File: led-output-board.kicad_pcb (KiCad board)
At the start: 2 copper layers, 29 parts, among them J1 DBT50G-9.5-2P, J10 DB301V-3.5-3P-GN, J2 Conn_02x08_Odd_Even, J3 DB301V-3.5-3P-GN, J4 DB301V-3.5-3P-GN, J5 DB301V-3.5-3P-GN, J6 DB301V-3.5-3P-GN, J7 DB301V-3.5-3P-GN, J8 DB301V-3.5-3P-GN, J9 DB301V-3.5-3P-GN, U1 SN74LVC8T245PWR

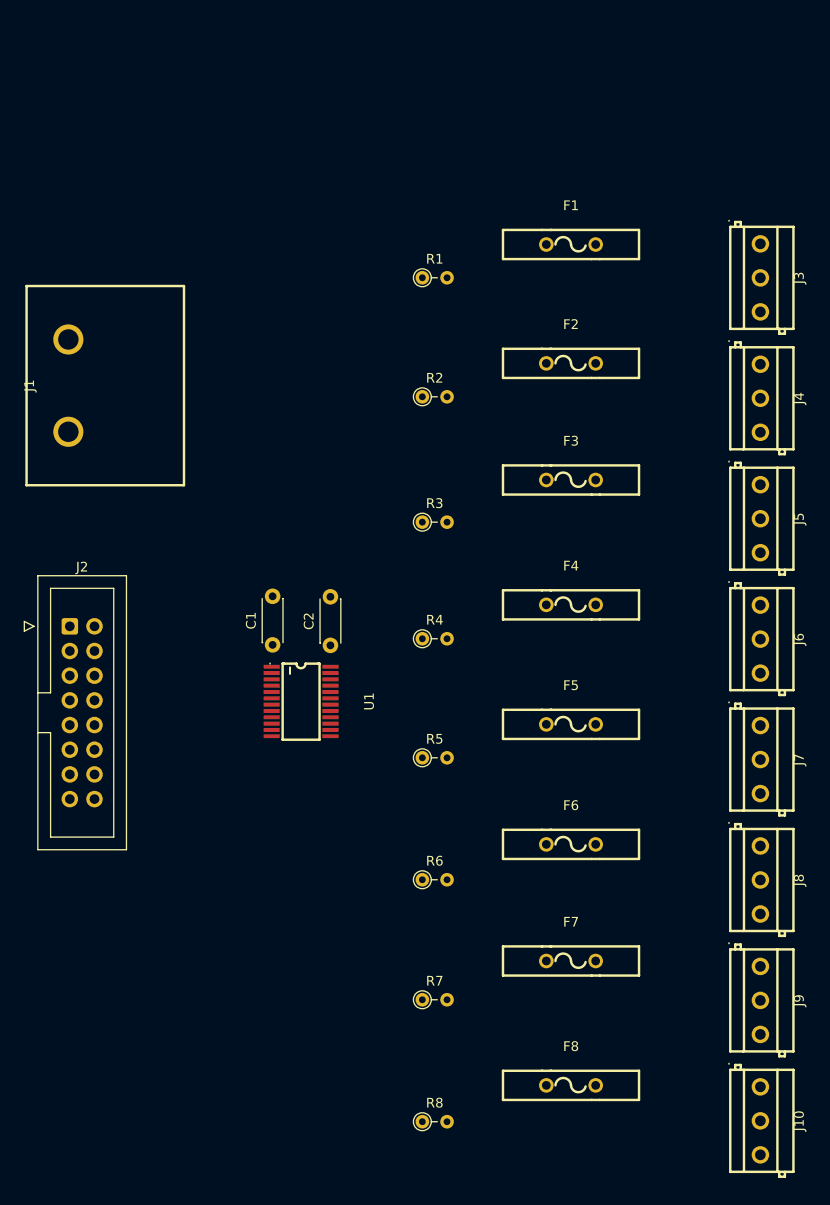
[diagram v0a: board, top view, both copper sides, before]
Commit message: Moving fuses closer
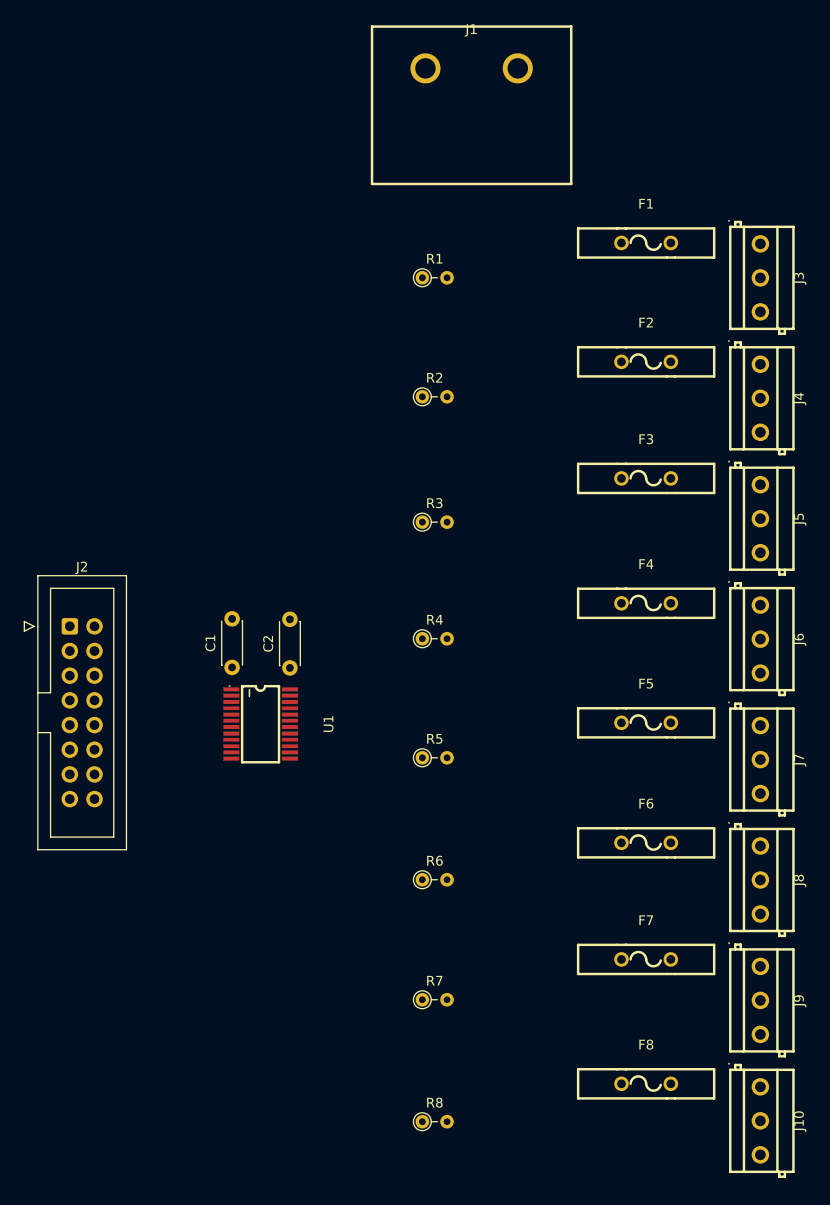
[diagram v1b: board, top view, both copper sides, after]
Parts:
- moved J1 52.8 mm to (107.9, 46.6), turned to 0 degrees
- moved F1 7.73 mm to (125.9, 64.6)
- moved F2 7.73 mm to (125.9, 76.8)
- moved F3 7.73 mm to (125.9, 88.8)
- moved F4 7.73 mm to (125.9, 101.7)
- moved F5 7.73 mm to (125.9, 114.0)
- moved F6 7.73 mm to (125.9, 126.3)
- moved F7 7.73 mm to (125.9, 138.3)
- moved F8 7.73 mm to (125.9, 151.2)
- moved C1 4.77 mm to (83.2, 108.3)
- moved C2 4.77 mm to (89.2, 108.3)
- moved U1 4.77 mm to (86.2, 114.1)
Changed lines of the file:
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@@
 	(footprint "easyeda2kicad:FUSE-TH_L14.0-W3.0-P5.08-D0.6"
 		(layer "F.Cu")
-		(at 118.1275 77.010357)
+		(at 125.86 76.85)
 		(property "Reference" "F2"
 			(at 0 -4 0)
@@
 	(footprint "easyeda2kicad:FUSE-TH_L14.0-W3.0-P5.08-D0.6"
 		(layer "F.Cu")
-		(at 118.1275 151.310357)
+		(at 125.86 151.15)
 		(property "Reference" "F8"
 			(at 0 -4 0)
@@
 	(footprint "easyeda2kicad:FUSE-TH_L14.0-W3.0-P5.08-D0.6"
 		(layer "F.Cu")
-		(at 118.1275 64.777857)
+		(at 125.86 64.6175)
 		(property "Reference" "F1"
 			(at 0 -4 0)
@@
 	(footprint "easyeda2kicad:CONN-TH_2P-P9.50_DBT50G-9.5-2P"
 		(layer "F.Cu")
-		(at 66.4 79.3 90)
+		(at 107.9 46.65)
 		(property "Reference" "J1"
-			(at 0 -4 90)
+			(at 0 -4 0)
 			(layer "F.SilkS")
 			(effects
@@
 		)
 		(property "Value" "DBT50G-9.5-2P"
-			(at 0 4 90)
+			(at 0 4 0)
 			(layer "F.Fab")
 			(effects
@@
 		)
 		(property "Datasheet" ""
-			(at 0 0 90)
+			(at 0 0 0)
 			(layer "F.Fab")
 			(hide yes)
@@
 		)
 		(property "Description" ""
-			(at 0 0 90)
+			(at 0 0 0)
 			(layer "F.Fab")
 			(hide yes)
@@
 		)
 		(property "LCSC Part" ""
-			(at 0 0 90)
+			(at 0 0 0)
 			(layer "F.Fab")
 			(hide yes)
@@
 		(duplicate_pad_numbers_are_jumpers no)
 		(fp_line
-			(start 10.25 -4.3)
-			(end -10.25 -4.3)
+			(start -10.25 -4.3)
+			(end -10.25 11.9)
 			(stroke
 				(width 0.25)
@@
 		)
 		(fp_line
-			(start -10.25 -4.3)
-			(end -10.25 11.9)
+			(start -10.25 11.9)
+			(end 10.25 11.9)
 			(stroke
 				(width 0.25)
@@
 		)
 		(fp_line
-			(start 10.25 11.9)
-			(end 10.25 -4.3)
+			(start 10.25 -4.3)
+			(end -10.25 -4.3)
 			(stroke
 				(width 0.25)
@@
 		)
 		(fp_line
-			(start -10.25 11.9)
-			(end 10.25 11.9)
+			(start 10.25 11.9)
+			(end 10.25 -4.3)
 			(stroke
 				(width 0.25)
@@
 		)
 		(fp_line
-			(start 10.25 -4.3)
-			(end 10.25 11.9)
+			(start -10.25 -4.3)
+			(end 10.25 -4.3)
 			(stroke
 				(width 0.05)
@@
 		)
 		(fp_line
-			(start -10.25 -4.3)
-			(end 10.25 -4.3)
+			(start -10.25 11.9)
+			(end -10.25 -4.3)
 			(stroke
 				(width 0.05)
@@
 		)
 		(fp_line
-			(start 10.25 11.9)
-			(end -10.25 11.9)
+			(start 10.25 -4.3)
+			(end 10.25 11.9)
 			(stroke
 				(width 0.05)
@@
 		)
 		(fp_line
-			(start -10.25 11.9)
-			(end -10.25 -4.3)
+			(start 10.25 11.9)
+			(end -10.25 11.9)
 			(stroke
 				(width 0.05)
@@
 		)
 		(fp_text user "${REFERENCE}"
-			(at 0 0 90)
+			(at 0 0 0)
 			(layer "F.Fab")
 			(effects
@@
 		)
 		(pad "1" thru_hole circle
-			(at -4.75 0 90)
+			(at -4.75 0)
 			(size 3.1 3.1)
 			(drill 2.100022)
@@
 		)
 		(pad "2" thru_hole circle
-			(at 4.75 0 90)
+			(at 4.75 0)
 			(size 3.1 3.1)
 			(drill 2.100022)
@@
 	(footprint "easyeda2kicad:FUSE-TH_L14.0-W3.0-P5.08-D0.6"
 		(layer "F.Cu")
-		(at 118.1275 89.010357)
+		(at 125.86 88.85)
 		(property "Reference" "F3"
 			(at 0 -4 0)
@@
 	(footprint "Capacitor_THT:C_Disc_D4.3mm_W1.9mm_P5.00mm"
 		(layer "F.Cu")
-		(at 87.42 105.98 90)
+		(at 83.25 108.3 90)
 		(descr "C, Disc series, Radial, pin pitch=5.00mm, diameter*width=4.3*1.9mm^2, Capacitor, http://www.vishay.com/docs/45233/krseries.pdf")
 		(tags "C Disc series Radial pin pitch 5.00mm diameter 4.3mm width 1.9mm Capacitor")
@@
 	(footprint "easyeda2kicad:FUSE-TH_L14.0-W3.0-P5.08-D0.6"
 		(layer "F.Cu")
-		(at 118.1275 101.860357)
+		(at 125.86 101.7)
 		(property "Reference" "F4"
 			(at 0 -4 0)
@@
 	(footprint "easyeda2kicad:FUSE-TH_L14.0-W3.0-P5.08-D0.6"
 		(layer "F.Cu")
-		(at 118.1275 126.510357)
+		(at 125.86 126.35)
 		(property "Reference" "F6"
 			(at 0 -4 0)
@@
 	(footprint "easyeda2kicad:TSSOP-24_L7.8-W4.4-P0.65-LS6.4-BL"
 		(layer "F.Cu")
-		(at 90.35 111.8 -90)
+		(at 86.18 114.12 -90)
 		(property "Reference" "U1"
 			(at 0 -7.023 90)
@@
 	(footprint "Capacitor_THT:C_Disc_D4.3mm_W1.9mm_P5.00mm"
 		(layer "F.Cu")
-		(at 93.37 106.03 90)
+		(at 89.2 108.35 90)
 		(descr "C, Disc series, Radial, pin pitch=5.00mm, diameter*width=4.3*1.9mm^2, Capacitor, http://www.vishay.com/docs/45233/krseries.pdf")
 		(tags "C Disc series Radial pin pitch 5.00mm diameter 4.3mm width 1.9mm Capacitor")
@@
 	(footprint "easyeda2kicad:FUSE-TH_L14.0-W3.0-P5.08-D0.6"
 		(layer "F.Cu")
-		(at 118.1275 114.160357)
+		(at 125.86 114)
 		(property "Reference" "F5"
 			(at 0 -4 0)
@@
 	(footprint "easyeda2kicad:FUSE-TH_L14.0-W3.0-P5.08-D0.6"
 		(layer "F.Cu")
-		(at 118.1275 138.510357)
+		(at 125.86 138.35)
 		(property "Reference" "F7"
 			(at 0 -4 0)

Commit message: Compacting output terminals
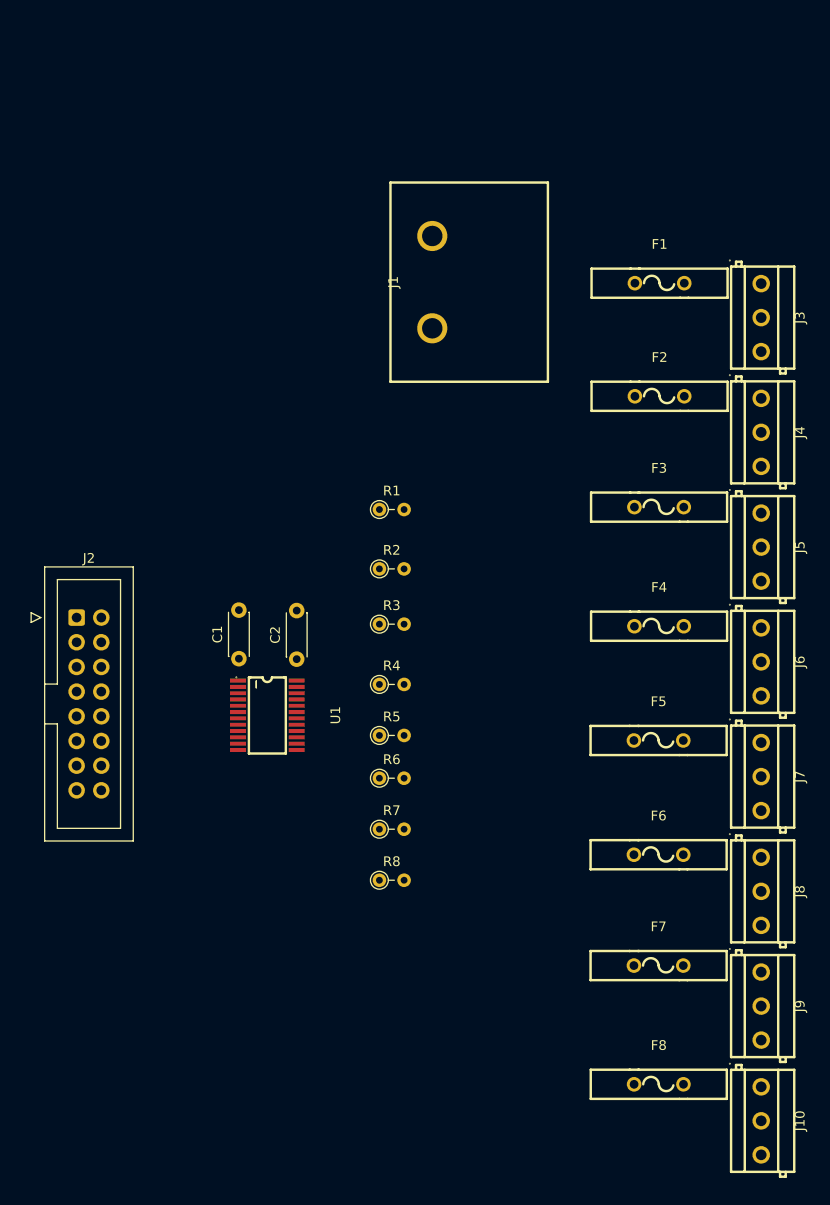
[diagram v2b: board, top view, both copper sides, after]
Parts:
- moved R8 25.2 mm to (98.4, 130.2)
- moved R1 24.3 mm to (98.4, 92.0)
- moved J1 22.4 mm to (103.8, 68.7), turned to 90 degrees
- moved R2 18.3 mm to (98.4, 98.2)
- moved R7 18.1 mm to (98.4, 125.0)
- moved R3 11.4 mm to (98.4, 103.8)
- moved R6 11.3 mm to (98.4, 119.7)
- moved R4 6.45 mm to (98.4, 110.0)
- moved R5 4.98 mm to (98.4, 115.3)
- moved F1 4.36 mm to (127.2, 68.8)
- moved J3 4.09 mm to (137.7, 72.3)
- moved F2 3.81 mm to (127.2, 80.4)
- moved J4 3.51 mm to (137.7, 84.1)
- moved F3 3.24 mm to (127.2, 91.8)
- moved J5 2.92 mm to (137.7, 95.9)
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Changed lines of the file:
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@@
 	(footprint "easyeda2kicad:FUSE-TH_L14.0-W3.0-P5.08-D0.6"
 		(layer "F.Cu")
-		(at 125.86 76.85)
+		(at 127.2425 80.396786)
 		(property "Reference" "F2"
 			(at 0 -4 0)
@@
 	(footprint "easyeda2kicad:FUSE-TH_L14.0-W3.0-P5.08-D0.6"
 		(layer "F.Cu")
-		(at 125.86 151.15)
+		(at 127.16 151.2)
 		(property "Reference" "F8"
 			(at 0 -4 0)
@@
 	(footprint "easyeda2kicad:FUSE-TH_L14.0-W3.0-P5.08-D0.6"
 		(layer "F.Cu")
-		(at 125.86 64.6175)
+		(at 127.2425 68.757143)
 		(property "Reference" "F1"
 			(at 0 -4 0)
@@
 	(footprint "Resistor_THT:R_Axial_DIN0204_L3.6mm_D1.6mm_P2.54mm_Vertical"
 		(layer "F.Cu")
-		(at 102.83 130.15)
+		(at 98.41 119.7)
 		(descr "Resistor, Axial_DIN0204 series, Axial, Vertical, pin pitch=2.54mm, 0.167W, length*diameter=3.6*1.6mm^2, http://cdn-reichelt.de/documents/datenblatt/B400/1_4W%23YAG.pdf")
 		(tags "Resistor Axial_DIN0204 series Axial Vertical pin pitch 2.54mm 0.167W length 3.6mm diameter 1.6mm")
@@
 	(footprint "Resistor_THT:R_Axial_DIN0204_L3.6mm_D1.6mm_P2.54mm_Vertical"
 		(layer "F.Cu")
-		(at 102.83 142.5)
+		(at 98.41 124.95)
 		(descr "Resistor, Axial_DIN0204 series, Axial, Vertical, pin pitch=2.54mm, 0.167W, length*diameter=3.6*1.6mm^2, http://cdn-reichelt.de/documents/datenblatt/B400/1_4W%23YAG.pdf")
 		(tags "Resistor Axial_DIN0204 series Axial Vertical pin pitch 2.54mm 0.167W length 3.6mm diameter 1.6mm")
@@
 	(footprint "Resistor_THT:R_Axial_DIN0204_L3.6mm_D1.6mm_P2.54mm_Vertical"
 		(layer "F.Cu")
-		(at 102.83 68.2)
+		(at 98.41 92.05)
 		(descr "Resistor, Axial_DIN0204 series, Axial, Vertical, pin pitch=2.54mm, 0.167W, length*diameter=3.6*1.6mm^2, http://cdn-reichelt.de/documents/datenblatt/B400/1_4W%23YAG.pdf")
 		(tags "Resistor Axial_DIN0204 series Axial Vertical pin pitch 2.54mm 0.167W length 3.6mm diameter 1.6mm")
@@
 	(footprint "Resistor_THT:R_Axial_DIN0204_L3.6mm_D1.6mm_P2.54mm_Vertical"
 		(layer "F.Cu")
-		(at 102.83 93.35)
+		(at 98.41 103.85)
 		(descr "Resistor, Axial_DIN0204 series, Axial, Vertical, pin pitch=2.54mm, 0.167W, length*diameter=3.6*1.6mm^2, http://cdn-reichelt.de/documents/datenblatt/B400/1_4W%23YAG.pdf")
 		(tags "Resistor Axial_DIN0204 series Axial Vertical pin pitch 2.54mm 0.167W length 3.6mm diameter 1.6mm")
@@
 	(footprint "Resistor_THT:R_Axial_DIN0204_L3.6mm_D1.6mm_P2.54mm_Vertical"
 		(layer "F.Cu")
-		(at 102.83 105.35)
+		(at 98.41 110.05)
 		(descr "Resistor, Axial_DIN0204 series, Axial, Vertical, pin pitch=2.54mm, 0.167W, length*diameter=3.6*1.6mm^2, http://cdn-reichelt.de/documents/datenblatt/B400/1_4W%23YAG.pdf")
 		(tags "Resistor Axial_DIN0204 series Axial Vertical pin pitch 2.54mm 0.167W length 3.6mm diameter 1.6mm")
@@
 	(footprint "easyeda2kicad:CONN-TH_DB301V-3.5-3P-GN"
 		(layer "F.Cu")
-		(at 137.6175 117.781786 -90)
+		(at 137.7 119.53449 -90)
 		(property "Reference" "J7"
 			(at 0 -4 90)
@@
 	(footprint "easyeda2kicad:CONN-TH_DB301V-3.5-3P-GN"
 		(layer "F.Cu")
-		(at 137.6175 92.996071 -90)
+		(at 137.7 95.917245 -90)
 		(property "Reference" "J5"
 			(at 0 -4 90)
@@
 	(footprint "Connector_IDC:IDC-Header_2x08_P2.54mm_Vertical"
 		(layer "F.Cu")
-		(at 66.55 104.07)
+		(at 67.25 103.17)
 		(descr "Through hole IDC box header, 2x08, 2.54mm pitch, DIN 41651 / IEC 60603-13, double rows, https://docs.google.com/spreadsheets/d/16SsEcesNF15N3Lb4niX7dcUr-NY5_MFPQhobNuNppn4/edit#gid=0")
 		(tags "Through hole vertical IDC box header THT 2x08 2.54mm double row")
@@
 	(footprint "easyeda2kicad:CONN-TH_2P-P9.50_DBT50G-9.5-2P"
 		(layer "F.Cu")
-		(at 107.9 46.65)
+		(at 103.85 68.65 90)
 		(property "Reference" "J1"
-			(at 0 -4 0)
+			(at 0 -4 90)
 			(layer "F.SilkS")
 			(effects
@@
 		)
 		(property "Value" "DBT50G-9.5-2P"
-			(at 0 4 0)
+			(at 0 4 90)
 			(layer "F.Fab")
 			(effects
@@
 		)
 		(property "Datasheet" ""
-			(at 0 0 0)
+			(at 0 0 90)
 			(layer "F.Fab")
 			(hide yes)
@@
 		)
 		(property "Description" ""
-			(at 0 0 0)
+			(at 0 0 90)
 			(layer "F.Fab")
 			(hide yes)
@@
 		)
 		(property "LCSC Part" ""
-			(at 0 0 0)
+			(at 0 0 90)
 			(layer "F.Fab")
 			(hide yes)
@@
 		(duplicate_pad_numbers_are_jumpers no)
 		(fp_line
-			(start -10.25 -4.3)
-			(end -10.25 11.9)
+			(start 10.25 -4.3)
+			(end -10.25 -4.3)
 			(stroke
 				(width 0.25)
@@
 		)
 		(fp_line
-			(start -10.25 11.9)
-			(end 10.25 11.9)
+			(start -10.25 -4.3)
+			(end -10.25 11.9)
 			(stroke
 				(width 0.25)
@@
 		)
 		(fp_line
-			(start 10.25 -4.3)
-			(end -10.25 -4.3)
+			(start 10.25 11.9)
+			(end 10.25 -4.3)
 			(stroke
 				(width 0.25)
@@
 		)
 		(fp_line
-			(start 10.25 11.9)
-			(end 10.25 -4.3)
+			(start -10.25 11.9)
+			(end 10.25 11.9)
 			(stroke
 				(width 0.25)
@@
 		)
 		(fp_line
-			(start -10.25 -4.3)
-			(end 10.25 -4.3)
+			(start 10.25 -4.3)
+			(end 10.25 11.9)
 			(stroke
 				(width 0.05)
@@
 		)
 		(fp_line
-			(start -10.25 11.9)
-			(end -10.25 -4.3)
+			(start -10.25 -4.3)
+			(end 10.25 -4.3)
 			(stroke
 				(width 0.05)
@@
 		)
 		(fp_line
-			(start 10.25 -4.3)
-			(end 10.25 11.9)
+			(start 10.25 11.9)
+			(end -10.25 11.9)
 			(stroke
 				(width 0.05)
@@
 		)
 		(fp_line
-			(start 10.25 11.9)
-			(end -10.25 11.9)
+			(start -10.25 11.9)
+			(end -10.25 -4.3)
 			(stroke
 				(width 0.05)
@@
 		)
 		(fp_text user "${REFERENCE}"
-			(at 0 0 0)
+			(at 0 0 90)
 			(layer "F.Fab")
 			(effects
@@
 		)
 		(pad "1" thru_hole circle
-			(at -4.75 0)
+			(at -4.75 0 90)
 			(size 3.1 3.1)
 			(drill 2.100022)
@@
 		)
 		(pad "2" thru_hole circle
-			(at 4.75 0)
+			(at 4.75 0 90)
 			(size 3.1 3.1)
 			(drill 2.100022)
@@
 	(footprint "easyeda2kicad:FUSE-TH_L14.0-W3.0-P5.08-D0.6"
 		(layer "F.Cu")
-		(at 125.86 88.85)
+		(at 127.1925 91.803929)
 		(property "Reference" "F3"
 			(at 0 -4 0)
@@
 	(footprint "easyeda2kicad:CONN-TH_DB301V-3.5-3P-GN"
 		(layer "F.Cu")
-		(at 137.6175 68.210357 -90)
+		(at 137.7 72.3 -90)
 		(property "Reference" "J3"
 			(at 0 -4 90)
@@
 	(footprint "Capacitor_THT:C_Disc_D4.3mm_W1.9mm_P5.00mm"
 		(layer "F.Cu")
-		(at 83.25 108.3 90)
+		(at 83.95 107.4 90)
 		(descr "C, Disc series, Radial, pin pitch=5.00mm, diameter*width=4.3*1.9mm^2, Capacitor, http://www.vishay.com/docs/45233/krseries.pdf")
 		(tags "C Disc series Radial pin pitch 5.00mm diameter 4.3mm width 1.9mm Capacitor")
@@
 	(footprint "easyeda2kicad:CONN-TH_DB301V-3.5-3P-GN"
 		(layer "F.Cu")
-		(at 137.6175 80.603214 -90)
+		(at 137.7 84.108622 -90)
 		(property "Reference" "J4"
 			(at 0 -4 90)
@@
 	(footprint "easyeda2kicad:FUSE-TH_L14.0-W3.0-P5.08-D0.6"
 		(layer "F.Cu")
-		(at 125.86 101.7)
+		(at 127.1925 104.061072)
 		(property "Reference" "F4"
 			(at 0 -4 0)
@@
 	(footprint "easyeda2kicad:CONN-TH_DB301V-3.5-3P-GN"
 		(layer "F.Cu")
-		(at 137.6175 142.5675 -90)
+		(at 137.7 143.151735 -90)
 		(property "Reference" "J9"
 			(at 0 -4 90)
@@
 	(footprint "Resistor_THT:R_Axial_DIN0204_L3.6mm_D1.6mm_P2.54mm_Vertical"
 		(layer "F.Cu")
-		(at 102.83 155.05)
+		(at 98.41 130.2)
 		(descr "Resistor, Axial_DIN0204 series, Axial, Vertical, pin pitch=2.54mm, 0.167W, length*diameter=3.6*1.6mm^2, http://cdn-reichelt.de/documents/datenblatt/B400/1_4W%23YAG.pdf")
 		(tags "Resistor Axial_DIN0204 series Axial Vertical pin pitch 2.54mm 0.167W length 3.6mm diameter 1.6mm")
@@
 	(footprint "easyeda2kicad:FUSE-TH_L14.0-W3.0-P5.08-D0.6"
 		(layer "F.Cu")
-		(at 125.86 126.35)
+		(at 127.1425 127.575357)
 		(property "Reference" "F6"
 			(at 0 -4 0)
@@
 	(footprint "easyeda2kicad:CONN-TH_DB301V-3.5-3P-GN"
 		(layer "F.Cu")
-		(at 137.6175 130.174643 -90)
+		(at 137.7 131.343112 -90)
 		(property "Reference" "J8"
 			(at 0 -4 90)
@@
 	(footprint "easyeda2kicad:CONN-TH_DB301V-3.5-3P-GN"
 		(layer "F.Cu")
-		(at 137.6175 105.388928 -90)
+		(at 137.7 107.725867 -90)
 		(property "Reference" "J6"
 			(at 0 -4 90)
@@
 	(footprint "easyeda2kicad:TSSOP-24_L7.8-W4.4-P0.65-LS6.4-BL"
 		(layer "F.Cu")
-		(at 86.18 114.12 -90)
+		(at 86.88 113.22 -90)
 		(property "Reference" "U1"
 			(at 0 -7.023 90)
@@
 	(footprint "Capacitor_THT:C_Disc_D4.3mm_W1.9mm_P5.00mm"
 		(layer "F.Cu")
-		(at 89.2 108.35 90)
+		(at 89.9 107.45 90)
 		(descr "C, Disc series, Radial, pin pitch=5.00mm, diameter*width=4.3*1.9mm^2, Capacitor, http://www.vishay.com/docs/45233/krseries.pdf")
 		(tags "C Disc series Radial pin pitch 5.00mm diameter 4.3mm width 1.9mm Capacitor")
@@
 	(footprint "easyeda2kicad:CONN-TH_DB301V-3.5-3P-GN"
 		(layer "F.Cu")
-		(at 137.6175 154.960357 -90)
+		(at 137.7 154.960357 -90)
 		(property "Reference" "J10"
 			(at 0 -4 90)
@@
 	(footprint "easyeda2kicad:FUSE-TH_L14.0-W3.0-P5.08-D0.6"
 		(layer "F.Cu")
-		(at 125.86 114)
+		(at 127.1425 115.818214)
 		(property "Reference" "F5"
 			(at 0 -4 0)
@@
 	(footprint "Resistor_THT:R_Axial_DIN0204_L3.6mm_D1.6mm_P2.54mm_Vertical"
 		(layer "F.Cu")
-		(at 102.83 117.6)
+		(at 98.41 115.3)
 		(descr "Resistor, Axial_DIN0204 series, Axial, Vertical, pin pitch=2.54mm, 0.167W, length*diameter=3.6*1.6mm^2, http://cdn-reichelt.de/documents/datenblatt/B400/1_4W%23YAG.pdf")
 		(tags "Resistor Axial_DIN0204 series Axial Vertical pin pitch 2.54mm 0.167W length 3.6mm diameter 1.6mm")
@@
 	(footprint "Resistor_THT:R_Axial_DIN0204_L3.6mm_D1.6mm_P2.54mm_Vertical"
 		(layer "F.Cu")
-		(at 102.83 80.45)
+		(at 98.41 98.16)
 		(descr "Resistor, Axial_DIN0204 series, Axial, Vertical, pin pitch=2.54mm, 0.167W, length*diameter=3.6*1.6mm^2, http://cdn-reichelt.de/documents/datenblatt/B400/1_4W%23YAG.pdf")
 		(tags "Resistor Axial_DIN0204 series Axial Vertical pin pitch 2.54mm 0.167W length 3.6mm diameter 1.6mm")
@@
 	(footprint "easyeda2kicad:FUSE-TH_L14.0-W3.0-P5.08-D0.6"
 		(layer "F.Cu")
-		(at 125.86 138.35)
+		(at 127.1425 138.9825)
 		(property "Reference" "F7"
 			(at 0 -4 0)
